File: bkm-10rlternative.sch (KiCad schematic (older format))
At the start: 0 parts

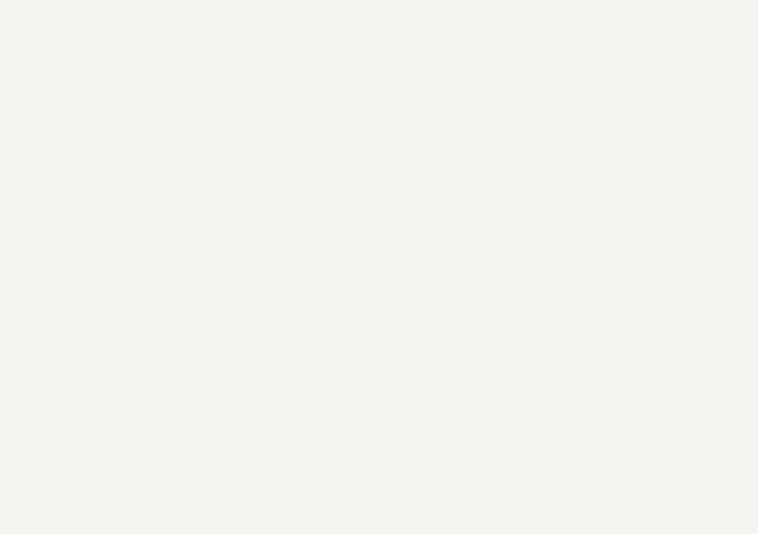
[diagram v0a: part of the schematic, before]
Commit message: Initial PCB routed
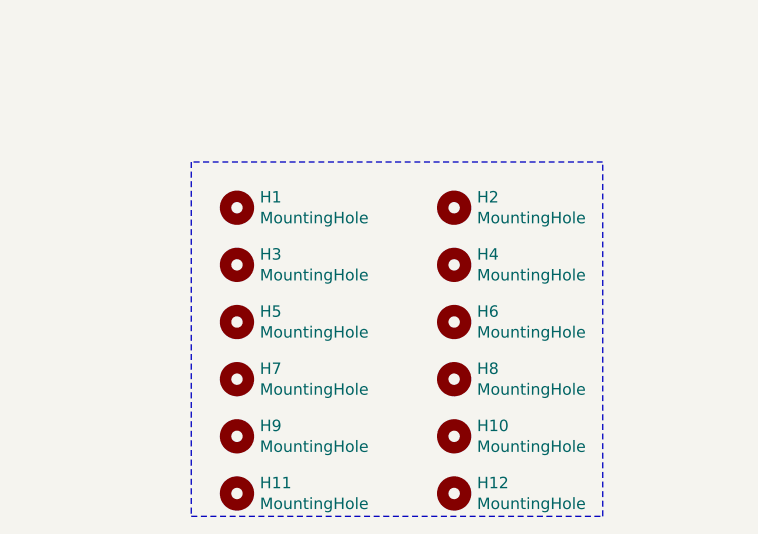
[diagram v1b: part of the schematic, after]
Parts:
- added H1, H10, H11, H12, H2, H3, H4, H5, H6, H7, H8, H9: MountingHole, MountingHole:MountingHole_3.2mm_M3, symbol Mechanical:MountingHole
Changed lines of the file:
@@
 F1 "mcu-rs485.sch" 50
 $EndSheet
+Wire Notes Line
+	7850 4500 7850 6050
+Wire Notes Line
+	7850 6050 9650 6050
+Wire Notes Line
+	9650 6050 9650 4500
+Wire Notes Line
+	9650 4500 7850 4500
+$Comp
+L Mechanical:MountingHole H1
+U 1 1 61881A08
+P 8050 4700
+F 0 "H1" H 8150 4746 50  0000 L CNN
+F 1 "MountingHole" H 8150 4655 50  0000 L CNN
+F 2 "MountingHole:MountingHole_3.2mm_M3" H 8050 4700 50  0001 C CNN
+F 3 "~" H 8050 4700 50  0001 C CNN
+	1    8050 4700
+	1    0    0    -1
+$EndComp
+$Comp
+L Mechanical:MountingHole H2
+U 1 1 61881CBE
+P 9000 4700
+F 0 "H2" H 9100 4746 50  0000 L CNN
+F 1 "MountingHole" H 9100 4655 50  0000 L CNN
+F 2 "MountingHole:MountingHole_3.2mm_M3" H 9000 4700 50  0001 C CNN
+F 3 "~" H 9000 4700 50  0001 C CNN
+	1    9000 4700
+	1    0    0    -1
+$EndComp
+$Comp
+L Mechanical:MountingHole H3
+U 1 1 61881EC0
+P 8050 4950
+F 0 "H3" H 8150 4996 50  0000 L CNN
+F 1 "MountingHole" H 8150 4905 50  0000 L CNN
+F 2 "MountingHole:MountingHole_3.2mm_M3" H 8050 4950 50  0001 C CNN
+F 3 "~" H 8050 4950 50  0001 C CNN
+	1    8050 4950
+	1    0    0    -1
+$EndComp
+$Comp
+L Mechanical:MountingHole H6
+U 1 1 6188209E
+P 9000 5200
+F 0 "H6" H 9100 5246 50  0000 L CNN
+F 1 "MountingHole" H 9100 5155 50  0000 L CNN
+F 2 "MountingHole:MountingHole_3.2mm_M3" H 9000 5200 50  0001 C CNN
+F 3 "~" H 9000 5200 50  0001 C CNN
+	1    9000 5200
+	1    0    0    -1
+$EndComp
+$Comp
+L Mechanical:MountingHole H7
+U 1 1 61882247
+P 8050 5450
+F 0 "H7" H 8150 5496 50  0000 L CNN
+F 1 "MountingHole" H 8150 5405 50  0000 L CNN
+F 2 "MountingHole:MountingHole_3.2mm_M3" H 8050 5450 50  0001 C CNN
+F 3 "~" H 8050 5450 50  0001 C CNN
+	1    8050 5450
+	1    0    0    -1
+$EndComp
+$Comp
+L Mechanical:MountingHole H4
+U 1 1 61884325
+P 9000 4950
+F 0 "H4" H 9100 4996 50  0000 L CNN
+F 1 "MountingHole" H 9100 4905 50  0000 L CNN
+F 2 "MountingHole:MountingHole_3.2mm_M3" H 9000 4950 50  0001 C CNN
+F 3 "~" H 9000 4950 50  0001 C CNN
+	1    9000 4950
+	1    0    0    -1
+$EndComp
+$Comp
+L Mechanical:MountingHole H5
+U 1 1 618845AF
+P 8050 5200
+F 0 "H5" H 8150 5246 50  0000 L CNN
+F 1 "MountingHole" H 8150 5155 50  0000 L CNN
+F 2 "MountingHole:MountingHole_3.2mm_M3" H 8050 5200 50  0001 C CNN
+F 3 "~" H 8050 5200 50  0001 C CNN
+	1    8050 5200
+	1    0    0    -1
+$EndComp
+$Comp
+L Mechanical:MountingHole H8
+U 1 1 6188A420
+P 9000 5450
+F 0 "H8" H 9100 5496 50  0000 L CNN
+F 1 "MountingHole" H 9100 5405 50  0000 L CNN
+F 2 "MountingHole:MountingHole_3.2mm_M3" H 9000 5450 50  0001 C CNN
+F 3 "~" H 9000 5450 50  0001 C CNN
+	1    9000 5450
+	1    0    0    -1
+$EndComp
+$Comp
+L Mechanical:MountingHole H9
+U 1 1 6188A792
+P 8050 5700
+F 0 "H9" H 8150 5746 50  0000 L CNN
+F 1 "MountingHole" H 8150 5655 50  0000 L CNN
+F 2 "MountingHole:MountingHole_3.2mm_M3" H 8050 5700 50  0001 C CNN
+F 3 "~" H 8050 5700 50  0001 C CNN
+	1    8050 5700
+	1    0    0    -1
+$EndComp
+$Comp
+L Mechanical:MountingHole H10
+U 1 1 6188A948
+P 9000 5700
+F 0 "H10" H 9100 5746 50  0000 L CNN
+F 1 "MountingHole" H 9100 5655 50  0000 L CNN
+F 2 "MountingHole:MountingHole_3.2mm_M3" H 9000 5700 50  0001 C CNN
+F 3 "~" H 9000 5700 50  0001 C CNN
+	1    9000 5700
+	1    0    0    -1
+$EndComp
+$Comp
+L Mechanical:MountingHole H11
+U 1 1 618B602D
+P 8050 5950
+F 0 "H11" H 8150 5996 50  0000 L CNN
+F 1 "MountingHole" H 8150 5905 50  0000 L CNN
+F 2 "MountingHole:MountingHole_3.2mm_M3" H 8050 5950 50  0001 C CNN
+F 3 "~" H 8050 5950 50  0001 C CNN
+	1    8050 5950
+	1    0    0    -1
+$EndComp
+$Comp
+L Mechanical:MountingHole H12
+U 1 1 618B8D04
+P 9000 5950
+F 0 "H12" H 9100 5996 50  0000 L CNN
+F 1 "MountingHole" H 9100 5905 50  0000 L CNN
+F 2 "MountingHole:MountingHole_3.2mm_M3" H 9000 5950 50  0001 C CNN
+F 3 "~" H 9000 5950 50  0001 C CNN
+	1    9000 5950
+	1    0    0    -1
+$EndComp
 $EndSCHEMATC
